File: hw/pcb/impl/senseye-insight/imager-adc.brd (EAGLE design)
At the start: 14.9 x 16.6 mm, 10 parts, among them J1 HEADER_12PIN2X6_NOSILK, U1 STONYMANDEFAULT_LENS_MOUNT, U2 TI_ADCXX1S101

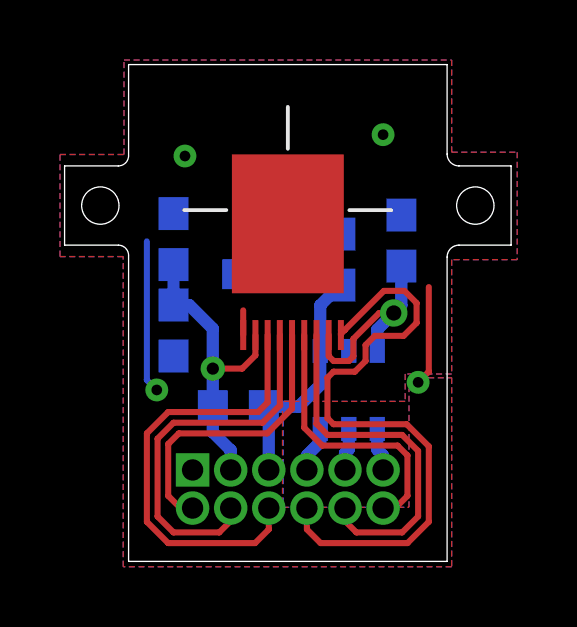
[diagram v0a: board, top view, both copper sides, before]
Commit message: updated board layout to bridge grounds beneath ADC
which is supposed to be good practice in mixed digital/analog design
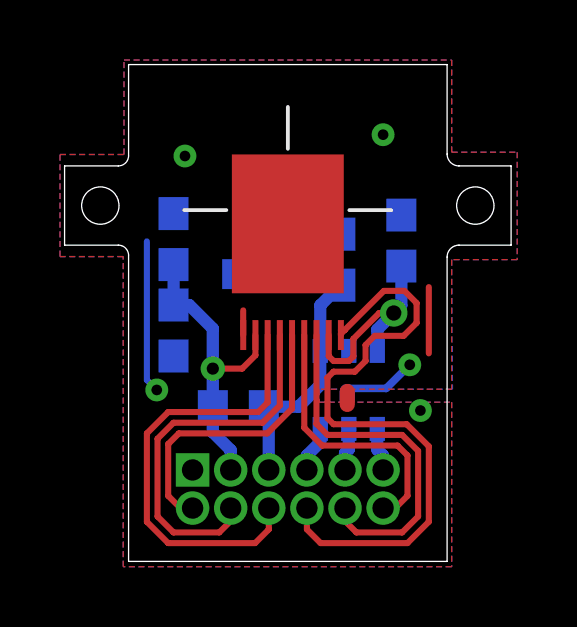
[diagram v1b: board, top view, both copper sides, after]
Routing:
- net GND: track 9.24 -> 11.3 mm, vias 4 -> 5
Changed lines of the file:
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@@
 <layer number="20" name="Dimension" color="15" fill="1" visible="yes" active="yes"/>
 <layer number="21" name="tPlace" color="7" fill="1" visible="yes" active="yes"/>
-<layer number="22" name="bPlace" color="7" fill="1" visible="yes" active="yes"/>
+<layer number="22" name="bPlace" color="7" fill="1" visible="no" active="yes"/>
 <layer number="23" name="tOrigins" color="15" fill="1" visible="yes" active="yes"/>
-<layer number="24" name="bOrigins" color="15" fill="1" visible="yes" active="yes"/>
+<layer number="24" name="bOrigins" color="15" fill="1" visible="no" active="yes"/>
 <layer number="25" name="tNames" color="7" fill="1" visible="yes" active="yes"/>
-<layer number="26" name="bNames" color="7" fill="1" visible="yes" active="yes"/>
+<layer number="26" name="bNames" color="7" fill="1" visible="no" active="yes"/>
 <layer number="27" name="tValues" color="7" fill="1" visible="no" active="yes"/>
 <layer number="28" name="bValues" color="7" fill="1" visible="no" active="yes"/>
-<layer number="29" name="tStop" color="7" fill="3" visible="yes" active="yes"/>
-<layer number="30" name="bStop" color="7" fill="6" visible="yes" active="yes"/>
+<layer number="29" name="tStop" color="7" fill="3" visible="no" active="yes"/>
+<layer number="30" name="bStop" color="7" fill="6" visible="no" active="yes"/>
 <layer number="31" name="tCream" color="7" fill="4" visible="no" active="yes"/>
 <layer number="32" name="bCream" color="7" fill="5" visible="no" active="yes"/>
@@
 <layer number="38" name="bTest" color="7" fill="1" visible="no" active="yes"/>
 <layer number="39" name="tKeepout" color="4" fill="11" visible="yes" active="yes"/>
-<layer number="40" name="bKeepout" color="1" fill="11" visible="yes" active="yes"/>
+<layer number="40" name="bKeepout" color="1" fill="11" visible="no" active="yes"/>
 <layer number="41" name="tRestrict" color="4" fill="10" visible="yes" active="yes"/>
-<layer number="42" name="bRestrict" color="1" fill="10" visible="yes" active="yes"/>
+<layer number="42" name="bRestrict" color="1" fill="10" visible="no" active="yes"/>
 <layer number="43" name="vRestrict" color="2" fill="10" visible="yes" active="yes"/>
 <layer number="44" name="Drills" color="7" fill="1" visible="no" active="yes"/>
@@
 <layer number="50" name="dxf" color="7" fill="1" visible="no" active="no"/>
 <layer number="51" name="tDocu" color="14" fill="1" visible="yes" active="yes"/>
-<layer number="52" name="bDocu" color="14" fill="1" visible="yes" active="yes"/>
+<layer number="52" name="bDocu" color="14" fill="1" visible="no" active="yes"/>
 <layer number="53" name="tGND_GNDA" color="7" fill="9" visible="no" active="no"/>
 <layer number="54" name="bGND_GNDA" color="1" fill="9" visible="no" active="no"/>
@@
 <vertex x="15.0876" y="10.0584"/>
 <vertex x="12.9032" y="10.0584"/>
-<vertex x="12.9032" y="6.2484"/>
-<vertex x="11.3538" y="6.2484"/>
-<vertex x="11.3538" y="5.334"/>
-<vertex x="7.2644" y="5.334"/>
-<vertex x="7.2644" y="1.8034"/>
-<vertex x="11.4808" y="1.8034"/>
-<vertex x="11.4808" y="6.1214"/>
-<vertex x="12.9032" y="6.1214"/>
+<vertex x="12.9032" y="5.7404"/>
+<vertex x="8.4836" y="5.7404"/>
+<vertex x="8.4836" y="5.3086"/>
+<vertex x="12.9032" y="5.3086"/>
 <vertex x="12.9032" y="-0.1778"/>
 <vertex x="1.9558" y="-0.1778"/>
@@
 <vertex x="15.0876" y="10.0584"/>
 <vertex x="12.9032" y="10.0584"/>
-<vertex x="12.9032" y="6.2484"/>
-<vertex x="11.3538" y="6.2484"/>
-<vertex x="11.3538" y="5.334"/>
-<vertex x="7.2898" y="5.334"/>
-<vertex x="7.2898" y="1.8034"/>
-<vertex x="11.4808" y="1.8034"/>
-<vertex x="11.4808" y="6.1214"/>
-<vertex x="12.9032" y="6.1214"/>
+<vertex x="12.9286" y="5.7404"/>
+<vertex x="8.4836" y="5.7404"/>
+<vertex x="8.4836" y="5.3086"/>
+<vertex x="12.9032" y="5.3086"/>
 <vertex x="12.9032" y="-0.1778"/>
 <vertex x="1.9558" y="-0.1778"/>
@@
 <vertex x="1.9812" y="13.5636"/>
 </polygon>
-<via x="11.7856" y="5.969" extent="1-16" drill="0.3556" diameter="0.254"/>
 <contactref element="C5" pad="2"/>
 <wire x1="3.0734" y1="5.715" x2="2.7432" y2="6.0452" width="0.2032" layer="16"/>
@@
 <contactref element="C3" pad="2"/>
 <contactref element="C4" pad="2"/>
-<wire x1="11.7856" y1="5.969" x2="12.1412" y2="6.3246" width="0.2032" layer="1"/>
-<wire x1="12.1412" y1="6.3246" x2="12.1412" y2="9.144" width="0.2032" layer="1"/>
+<wire x1="12.1412" y1="6.9342" x2="12.1412" y2="9.144" width="0.2032" layer="1"/>
+<via x="11.5062" y="6.5532" extent="1-16" drill="0.3556"/>
+<via x="11.8618" y="5.0292" extent="1-16" drill="0.3556"/>
+<wire x1="9.4234" y1="5.6642" x2="9.4234" y2="5.2324" width="0.508" layer="1"/>
+<wire x1="9.4234" y1="5.6642" x2="9.4234" y2="5.3848" width="0.508" layer="16"/>
+<wire x1="9.4234" y1="5.715" x2="9.4234" y2="5.6642" width="0.254" layer="16"/>
+<wire x1="11.5062" y1="6.5532" x2="10.7188" y2="5.7658" width="0.254" layer="16"/>
+<wire x1="10.7188" y1="5.7658" x2="9.4234" y2="5.7658" width="0.254" layer="16"/>
+<wire x1="9.4234" y1="5.7658" x2="9.4234" y2="5.715" width="0.254" layer="16"/>
 </signal>
 <signal name="V_STONY">
